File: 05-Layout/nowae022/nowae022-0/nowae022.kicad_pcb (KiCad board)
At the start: 2 copper layers, 80 x 69.3 mm, 53 parts, among them P1 SUPPLY, P2 SWD, Q1 BCW66GLT, Q2 BCW66GLT, Q3 BCW66GLT, Q4 BCW66GLT, Q5 BCW66GLT, Q6 BCW66GLT, SW1 BUTTON-WE_434153017835, U1 MKL15Z128VFM4, U2 TPS70933DBV, Y1 32768

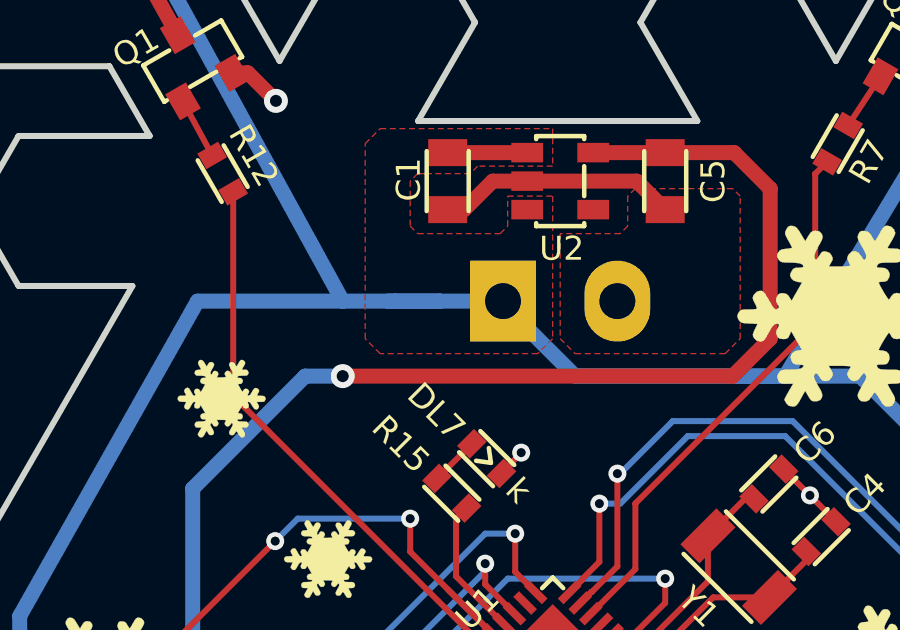
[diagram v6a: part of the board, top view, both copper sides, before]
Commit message: Fixed PCB silkscreen (nowae022-0)
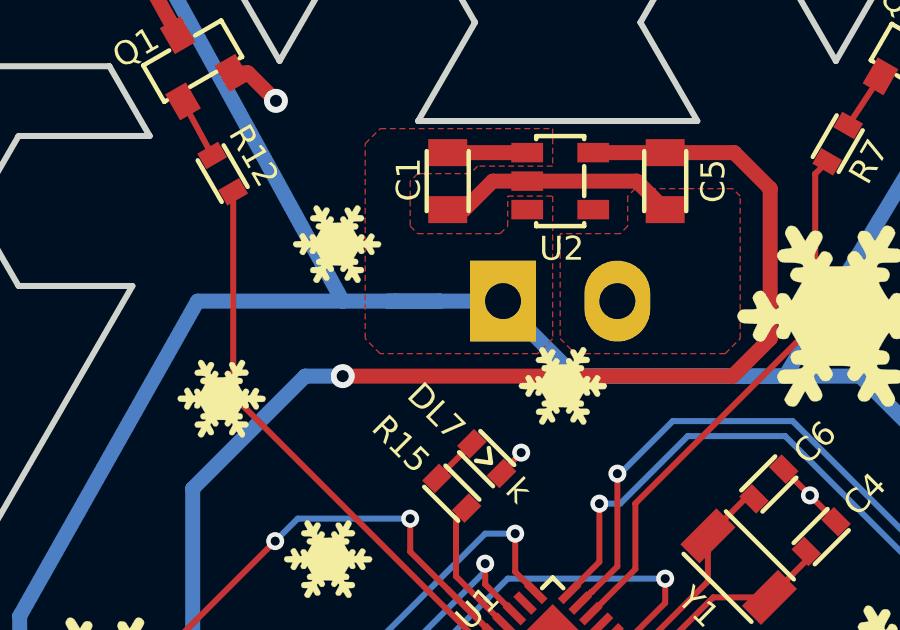
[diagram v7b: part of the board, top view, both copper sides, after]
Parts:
- added G***: LOGO, EXTLOGO:LOGO_SNOW1_3MM_FSILK, F.Cu at (132.8, 80.3)
- added G***: LOGO, EXTLOGO:LOGO_SNOW1_3MM_FSILK, F.Cu at (140.3, 85.1)
